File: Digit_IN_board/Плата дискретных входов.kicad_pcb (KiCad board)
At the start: 2 copper layers, 85 x 64.5 mm, 185 parts, among them J1 Prog, J2 Conn_01x02_Pin, J3 DS1013-01-14RSiB-B (1), J4 DS1013-01-10RSiB-B (1), J5 DS1013-01-10RSiB-B (2), J6 Conn_01x02_Pin, Q1 DTC114ECA, Q10 DTC114ECA (SOT-23), Q2 DTC114ECA, Q3 Si2309CDS (SOT-23), Q4 Si2309CDS (SOT-23), Q5 DTC114ECA (SOT-23), Q6 Si2309CDS (SOT-23), Q7 DTC114ECA (SOT-23), Q8 DTC114ECA (SOT-23), Q9 Si2309CDS (SOT-23), U1 ADM3485EARZ-REEL, U2 ISO6741FDWR, U3 STM32G070RBTx, U4 AM1SS-2403SJZ, U5 HEF40106B, U6 HEF40106B, U7 HEF40106B

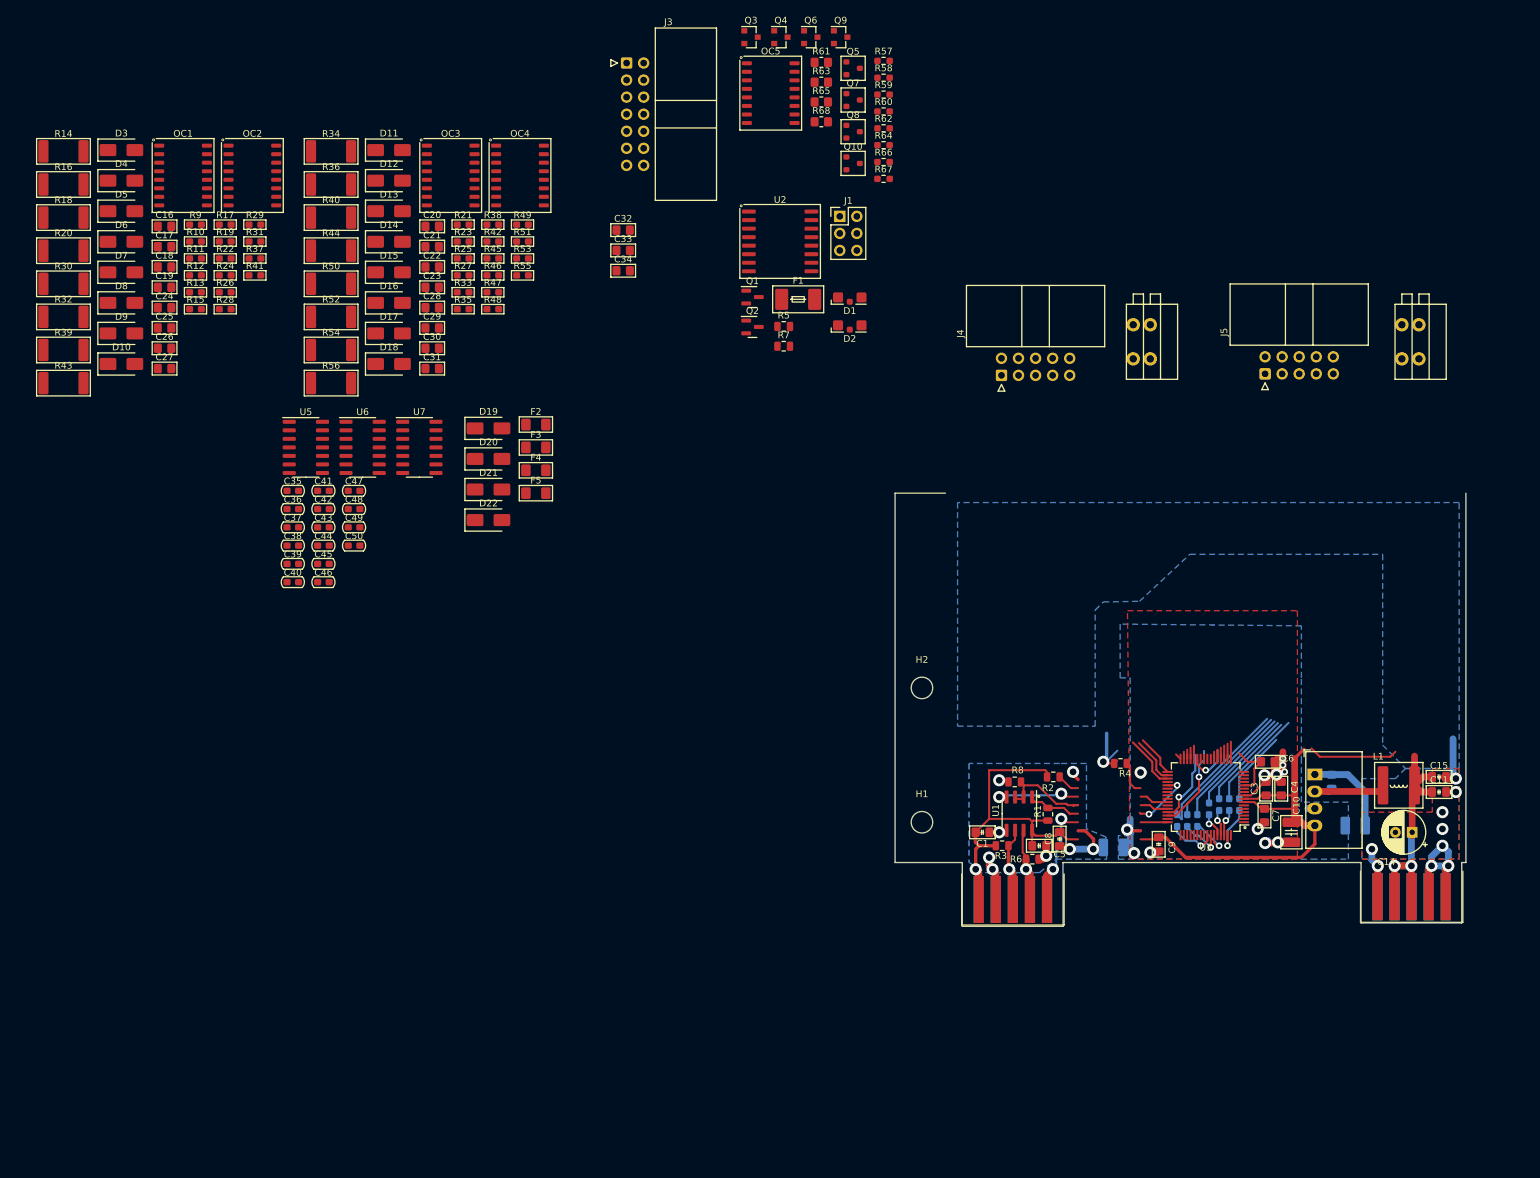
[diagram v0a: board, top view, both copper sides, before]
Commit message: Discret IN OUT schems
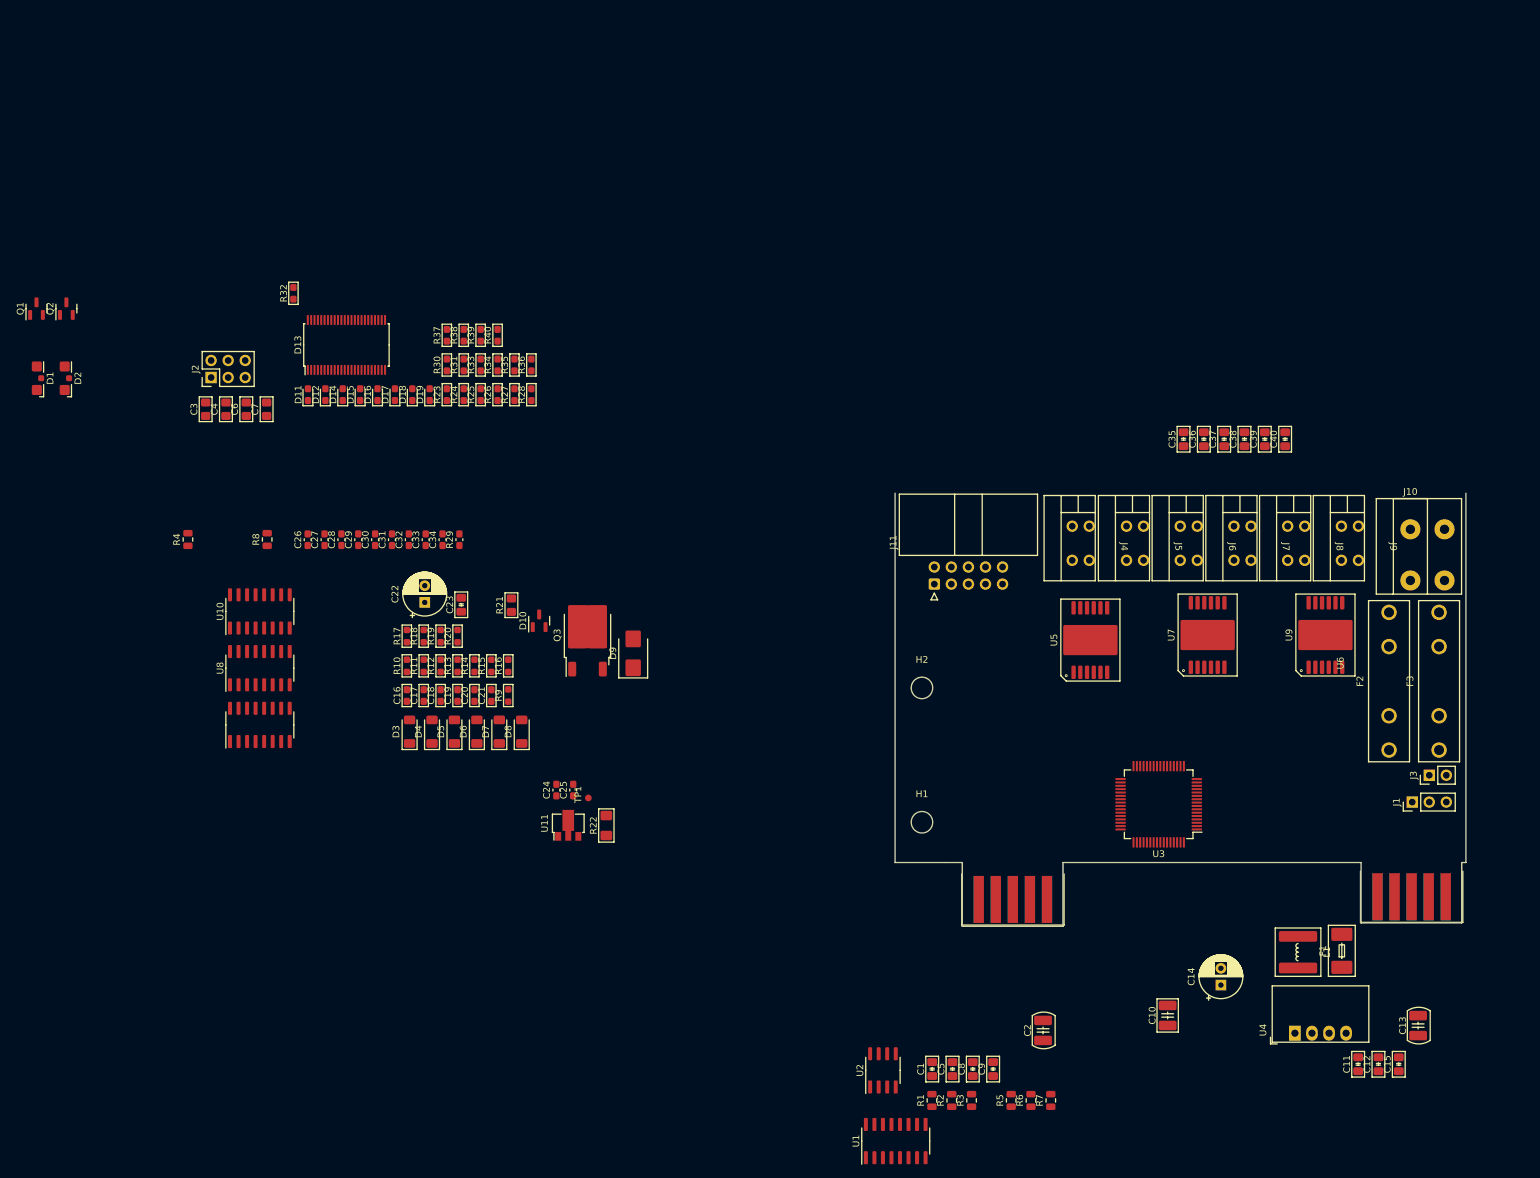
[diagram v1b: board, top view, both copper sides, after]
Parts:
- removed C41, C42, C43, C44, C45, C46, C47, C48, C49, C50: 0,01uF 50V 0603, PCM_Capacitor_SMD_US_Handsoldering_AKL:C_0603_1608Metric_Pad1.08x0.95mm
- removed D20, D21, D22: SMAJ26A, Diode_SMD:D_SMA
- removed F4, F5: 0466.500NRHF (0,5А 1206), PCM_Resistor_SMD_AKL:R_1206_3216Metric_Pad1.42x1.75mm_HandSolder
- removed OC1, OC2, OC3, OC4, OC5: IS281- 4, PCM_Package_SO_AKL:SOIC-16W_5.3x10.2mm_P1.27mm
- removed Q10, Q5, Q7, Q8: DTC114ECA (SOT-23), PCM_Package_TO_SOT_SMD_AKL:SOT-23
- removed Q4, Q6, Q9: Si2309CDS (SOT-23), PCM_4ms_Package_SOT:SOT-23
- removed the R40 at (5.02, 25.0)
- removed the R40 at (135.8, 113.0)
- removed R41, R42 (x2), R44, R45, R46 (x2), R47, R48 (x2), R49, R50, R51, R52, R53, R55: 102 0603, PCM_Resistor_SMD_AKL:R_0603_1608Metric_Pad1.05x0.95mm_HandSolder
- removed R43, R44, R50, R52, R54, R56: 102 2512, PCM_Resistor_SMD_AKL:R_2512_6332Metric_Pad1.52x3.35mm_HandSolder
- removed R57, R59, R62, R66: 103 0603, Resistor_SMD:R_0603_1608Metric_Pad0.98x0.95mm_HandSolder
- removed R58, R60, R64, R67: 473 0603, Resistor_SMD:R_0603_1608Metric_Pad0.98x0.95mm_HandSolder
- removed R61, R63, R65, R68: 201 0805, Resistor_SMD:R_0805_2012Metric_Pad1.20x1.40mm_HandSolder
- added J10: DG142R-5.08-02P-14, Connector:DG142R-5.08-02P-14, F.Cu at (165.7, 71.4)
- added J11: DS1013-01-10RSiB-B (1), Connector_IDC:IDC-Header_2x05_P2.54mm_Horizontal, F.Cu at (94.8, 79.5)
- added J7: DG141R-02, Connector:DG141R-02, F.Cu at (146.7, 74.0)
- added J8: DG141R-02, Connector:DG141R-02, F.Cu at (154.7, 74.0)
- added J9: DG141R-02, Connector:DG141R-02, F.Cu at (162.7, 74.0)
- added R40: 123 0603, PCM_Resistor_SMD_AKL:R_0603_1608Metric_Pad1.05x0.95mm_HandSolder, F.Cu at (29.8, 42.5)
- added TP1: TestPoint, PCM_4ms_TestPoint:TestPoint_D1, F.Cu at (43.3, 111.4)
- added U10: π162M30, Package_SO:SOIC-16_3.9x9.9mm_P1.27mm, F.Cu at (-5.59, 83.6)
- added U11: L78L05 (SOT89-3), Package_TO_SOT_SMD:SOT-89-3, F.Cu at (40.3, 115.2)
- added U8: π162M30, Package_SO:SOIC-16_3.9x9.9mm_P1.27mm, F.Cu at (-5.59, 92.1)
- added U9: BTS5215, PCM_Package_SO_AKL:Infineon_PG-DSO-12-9, F.Cu at (153.1, 87.1)
- C12, C13, C2: moved to F.Cu
- C16, C19, C21: value 0.1uF 100V 0805 -> 0,1uF 50V 0603; footprint PCM_Resistor_SMD_AKL:R_0805_2012Metric_Pad1.20x1.40mm_HandSolder -> PCM_Capacitor_SMD_AKL:C_0603_1608Metric_Pad1.08x0.95mm_HandSolder
- C17, C18, C20: value 0.1uF 100V 0805 -> 0,1uF 100V 0603; footprint PCM_Resistor_SMD_AKL:R_0805_2012Metric_Pad1.20x1.40mm_HandSolder -> PCM_Capacitor_SMD_AKL:C_0603_1608Metric_Pad1.08x0.95mm_HandSolder
- C22: value 0.1uF 100V 0805 -> 47uF 63V D10,5; footprint PCM_Resistor_SMD_AKL:R_0805_2012Metric_Pad1.20x1.40mm_HandSolder -> PCM_Capacitor_THT_AKL:CP_Radial_D6.3mm_P2.50mm
- C23: value 0.1uF 100V 0805 -> 0,1uF 100V 0805; footprint PCM_Resistor_SMD_AKL:R_0805_2012Metric_Pad1.20x1.40mm_HandSolder -> PCM_Capacitor_SMD_AKL:C_0805_2012Metric_Pad1.18x1.45mm_HandSolder
- C24: value 0.1uF 100V 0805 -> 0.33uF 50V 0603; footprint PCM_Resistor_SMD_AKL:R_0805_2012Metric_Pad1.20x1.40mm_HandSolder -> Capacitor_SMD:C_0603_1608Metric_Pad1.08x0.95mm_HandSolder
- C25: value 0.1uF 100V 0805 -> 0,1uF 50V 0603; footprint PCM_Resistor_SMD_AKL:R_0805_2012Metric_Pad1.20x1.40mm_HandSolder -> Capacitor_SMD:C_0603_1608Metric_Pad1.08x0.95mm_HandSolder
- C26, C27, C29, C30, C31, C32, C33, C34: value 0.1uF 100V 0805 -> 0,1uF 100V 0603; footprint PCM_Resistor_SMD_AKL:R_0805_2012Metric_Pad1.20x1.40mm_HandSolder -> Capacitor_SMD:C_0603_1608Metric_Pad1.08x0.95mm_HandSolder
- C28: value 0.1uF 100V 0805 -> 0,33uF 50V 0603; footprint PCM_Resistor_SMD_AKL:R_0805_2012Metric_Pad1.20x1.40mm_HandSolder -> Capacitor_SMD:C_0603_1608Metric_Pad1.08x0.95mm_HandSolder
- C35, C36, C37, C38, C39, C40: value 0,01uF 50V 0603 -> 0,1uF 100V 0805; footprint PCM_Capacitor_SMD_US_Handsoldering_AKL:C_0603_1608Metric_Pad1.08x0.95mm -> PCM_Capacitor_SMD_AKL:C_0805_2012Metric_Pad1.18x1.45mm_HandSolder
- D10: value SMAJ26A -> BZX84C10 (SOT-23); footprint Diode_SMD:D_SMA -> Package_TO_SOT_SMD:SOT-23
- D11, D12, D14, D15, D16, D17, D18, D19: value SMAJ26A -> LED 0603 (FYLS-0603UWC); footprint Diode_SMD:D_SMA -> LED_SMD:LED_0603_1608Metric_Pad1.05x0.95mm_HandSolder
- D13: value SMAJ26A -> ISO1I811T; footprint Diode_SMD:D_SMA -> Package_SO:TSSOP-48_6.1x12.5mm_P0.5mm
- D3, D4, D5, D6, D7, D8: value SMAJ26A -> BZV55B5V1; footprint Diode_SMD:D_SMA -> Diode_SMD:D_MiniMELF
- D9: value SMAJ26A -> SM6T30A (SMB); footprint Diode_SMD:D_SMA -> Diode_SMD:D_SMB
- F1: value 0452.500MRL -> 045201.5MRL
- F2, F3: value 0466.500NRHF (0,5А 1206) -> Fuse 5A ZH266 (2 клипсы); footprint PCM_Resistor_SMD_AKL:R_1206_3216Metric_Pad1.42x1.75mm_HandSolder -> Fuse:Fuseholder_100_series_5x20mm_D1,5
- J1: value Prog -> DebugUSART (PinHeader_01x03_P2.54mm); footprint Connector_PinHeader_2.54mm:PinHeader_2x03_P2.54mm_Vertical -> Connector_PinHeader_2.54mm:PinHeader_1x03_P2.54mm_Vertical
- J2: value Conn_01x02_Pin -> Prog (PinHeader_2x03_P2.54mm); footprint Connector:DG141V-2.54-02P -> Connector_PinHeader_2.54mm:PinHeader_2x03_P2.54mm_Vertical
- J3: value DS1013-01-14RSiB-B (1) -> Debug GPIO (PinHeader_01x02_P2.54mm); footprint Connector_IDC:IDC-Header_2x07_P2.54mm_Horizontal -> Connector_PinHeader_2.54mm:PinHeader_1x02_P2.54mm_Vertical
- J4: value DS1013-01-10RSiB-B (1) -> DG141R-02; footprint Connector_IDC:IDC-Header_2x05_P2.54mm_Horizontal -> Connector:DG141R-02
- J5: value DS1013-01-10RSiB-B (2) -> DG141R-02; footprint Connector_IDC:IDC-Header_2x05_P2.54mm_Horizontal -> Connector:DG141R-02
- J6: value Conn_01x02_Pin -> DG141R-02; footprint Connector:DG141V-2.54-02P -> Connector:DG141R-02
- Q1, Q2: value DTC114ECA -> DTC114ECA (SOT-23)
- Q3: value Si2309CDS (SOT-23) -> IRFR5305 (TO-252-2); footprint PCM_4ms_Package_SOT:SOT-23 -> Package_TO_SOT_SMD:TO-252-2
- R10, R11, R15, R19: value 102 0603 -> 123 0603; footprint PCM_Resistor_SMD_AKL:R_0603_1608Metric_Pad1.05x0.95mm_HandSolder -> PCM_Resistor_SMD_AKL:R_0603_1608Metric_Pad0.98x0.95mm_HandSolder
- R12: value 102 0603 -> 103 0603; footprint PCM_Resistor_SMD_AKL:R_0603_1608Metric_Pad1.05x0.95mm_HandSolder -> PCM_Resistor_SMD_AKL:R_0603_1608Metric_Pad0.98x0.95mm_HandSolder
- R13, R17, R9: value 102 0603 -> 302 0603; footprint PCM_Resistor_SMD_AKL:R_0603_1608Metric_Pad1.05x0.95mm_HandSolder -> PCM_Resistor_SMD_AKL:R_0603_1608Metric_Pad0.98x0.95mm_HandSolder
- R14, R18: value 102 2512 -> 123 0603; footprint PCM_Resistor_SMD_AKL:R_2512_6332Metric_Pad1.52x3.35mm_HandSolder -> PCM_Resistor_SMD_AKL:R_0603_1608Metric_Pad0.98x0.95mm_HandSolder
- R16, R20: value 102 2512 -> 103 0603; footprint PCM_Resistor_SMD_AKL:R_2512_6332Metric_Pad1.52x3.35mm_HandSolder -> PCM_Resistor_SMD_AKL:R_0603_1608Metric_Pad0.98x0.95mm_HandSolder
- R21: value 102 0603 -> 103 0805; footprint PCM_Resistor_SMD_AKL:R_0603_1608Metric_Pad1.05x0.95mm_HandSolder -> PCM_Resistor_SMD_AKL:R_0805_2012Metric_Pad1.20x1.40mm_HandSolder
- R22: value 102 0603 -> 621 1206; footprint PCM_Resistor_SMD_AKL:R_0603_1608Metric_Pad1.05x0.95mm_HandSolder -> PCM_Resistor_SMD_AKL:R_1206_3216Metric_Pad1.42x1.75mm_HandSolder
- R23, R25, R27, R33, R35, R37: value 102 0603 -> 202 0603
- R24, R26, R28, R31, R38: value 102 0603 -> 123 0603
- R29: value 102 0603 -> 204 0603; footprint PCM_Resistor_SMD_AKL:R_0603_1608Metric_Pad1.05x0.95mm_HandSolder -> Capacitor_SMD:C_0603_1608Metric_Pad1.08x0.95mm_HandSolder
- R30, R39: value 102 2512 -> 202 0603; footprint PCM_Resistor_SMD_AKL:R_2512_6332Metric_Pad1.52x3.35mm_HandSolder -> PCM_Resistor_SMD_AKL:R_0603_1608Metric_Pad1.05x0.95mm_HandSolder
- R32: value 102 2512 -> 330 0603; footprint PCM_Resistor_SMD_AKL:R_2512_6332Metric_Pad1.52x3.35mm_HandSolder -> PCM_Resistor_SMD_AKL:R_0603_1608Metric_Pad1.05x0.95mm_HandSolder
- R34, R36: value 102 2512 -> 123 0603; footprint PCM_Resistor_SMD_AKL:R_2512_6332Metric_Pad1.52x3.35mm_HandSolder -> PCM_Resistor_SMD_AKL:R_0603_1608Metric_Pad1.05x0.95mm_HandSolder
- R4: value 472 0805 -> 151 0805
- R5: value 151 0805 -> 472 0805
- R7: value 151 0805 -> 103 0805
- R8: value 103 0805 -> 151 0805
- U1: value ADM3485EARZ-REEL -> π141M3x; footprint Package_SO:SOIC-8_3.9x4.9mm_P1.27mm -> Package_SO:SOIC-16_3.9x9.9mm_P1.27mm
- U2: value ISO6741FDWR -> ADM3485EARZ-REEL (SOIC-8); footprint PCM_Package_SO_AKL:SOIC-16W_7.5x10.3mm_P1.27mm -> Package_SO:SOIC-8_3.9x4.9mm_P1.27mm
- U3: value STM32G070RBTx -> STM32G070RBTx (LQFP-64)
- U5, U7: value HEF40106B -> BTS5215; footprint Package_SO:SO-14_3.9x8.65mm_P1.27mm -> PCM_Package_SO_AKL:Infineon_PG-DSO-12-9
- U6: value HEF40106B -> π162M30; footprint Package_SO:SO-14_3.9x8.65mm_P1.27mm -> Package_SO:SOIC-16_3.9x9.9mm_P1.27mm
- moved C3 167.7 mm to (-13.7, 53.5)
- moved C4 167.0 mm to (-10.6, 53.5)
- moved C6 160.9 mm to (-7.61, 53.5), turned to 90 degrees
- moved C7 160.4 mm to (-4.59, 53.5), turned to 90 degrees
- moved J3 159.8 mm to (168.5, 108.0), turned to 90 degrees
- moved C40 149.3 mm to (147.1, 58.0), turned to 90 degrees
- moved C39 145.9 mm to (144.1, 58.0), turned to 90 degrees
- moved R4 142.8 mm to (-16.3, 72.9), turned to 90 degrees
- moved C38 142.6 mm to (141.0, 58.0), turned to 90 degrees
- moved F3 141.8 mm to (170.0, 104.2), turned to 90 degrees
- moved C37 139.3 mm to (138.0, 58.0), turned to 90 degrees
- moved J2 137.5 mm to (-12.8, 48.8), turned to 90 degrees
- moved C36 136.1 mm to (135.0, 58.0), turned to 90 degrees
- moved F2 136.0 mm to (162.6, 104.2), turned to 90 degrees
- moved C35 132.9 mm to (131.9, 58.0), turned to 90 degrees
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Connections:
- C16 pad 1: /IN_Detector/OUT1_1 -> GNDD
- C16 pad 2: GNDA -> +3V3
- C17 pad 1: /IN_Detector/OUT1_2 -> GND2
- C17 pad 2: GNDA -> +5V
- C18 pad 1: /IN_Detector/OUT1_3 -> GND2
- C18 pad 2: GNDA -> +5V
- C19 pad 1: /IN_Detector/OUT1_4 -> GNDD
- C19 pad 2: GNDA -> +3V3
- C20 pad 1: /IN_Detector/OUT2_1 -> GND2
- C20 pad 2: GNDA -> +5V
- C21 pad 1: /IN_Detector/OUT2_2 -> GNDD
- C21 pad 2: GNDA -> +3V3
- C22 pad 1: /IN_Detector/OUT2_3 -> +24V
- C22 pad 2: GNDA -> GND2
- C23 pad 1: /IN_Detector/OUT2_4 -> +24V
- C23 pad 2: GNDA -> GND2
- C24 pad 1: /IN_Detector/OUT1_5 -> Net-(U11-IN)
- C24 pad 2: GNDA -> GND2
- C25 pad 1: /IN_Detector/OUT1_6 -> +5V
- C25 pad 2: GNDA -> GND2
- C26 pad 1: /IN_Detector/OUT1_7 -> /Descret Input/OUT1_1
- C26 pad 2: GNDA -> GND2
- C27 pad 1: /IN_Detector/OUT1_8 -> /Descret Input/OUT1_2
- C27 pad 2: GNDA -> GND2
- C28 pad 1: /IN_Detector/OUT2_5 -> +3V3
- C28 pad 2: GNDA -> GNDD
- C29 pad 1: /IN_Detector/OUT2_6 -> /Descret Input/OUT1_3
- C29 pad 2: GNDA -> GND2
- C30 pad 1: /IN_Detector/OUT2_7 -> /Descret Input/OUT1_4
- C30 pad 2: GNDA -> GND2
- C31 pad 1: /IN_Detector/OUT2_8 -> /Descret Input/OUT1_5
- C31 pad 2: GNDA -> GND2
- C32 pad 1: +3V3 -> /Descret Input/OUT1_6
- C32 pad 2: GNDD -> GND2
- C33 pad 1: +3V3 -> /Descret Input/OUT1_7
- C33 pad 2: GNDD -> GND2
- C34 pad 1: +3V3 -> /Descret Input/OUT1_8
- C34 pad 2: GNDD -> GND2
- C35 pad 1: /IN_Detector/D2_1 -> GND2
- C35 pad 2: GNDD -> /+24_FT_1
- C36 pad 1: /IN_Detector/D2_2 -> GND2
- C36 pad 2: GNDD -> /DiscretOut/OUT2
- C37 pad 1: /IN_Detector/D2_3 -> GND2
- C37 pad 2: GNDD -> /DiscretOut/OUT3
- C38 pad 1: /IN_Detector/D2_4 -> GND2
- C38 pad 2: GNDD -> /DiscretOut/OUT4
- C39 pad 1: /IN_Detector/D2_5 -> GND2
- C39 pad 2: GNDD -> /DiscretOut/OUT5
- C40 pad 1: /IN_Detector/D2_6 -> GND2
- C40 pad 2: GNDD -> /DiscretOut/OUT6
- D10 pad 1: /IN_Detector/OUT1_8 -> Net-(D10-A)
- D10 pad 2: GNDA -> unconnected-(D10-NC-Pad2)
- D11 pad 1: /IN_Detector/OUT2_1 -> GND2
- D11 pad 2: GNDA -> /Descret Input/OUT1_L
- D12 pad 1: /IN_Detector/OUT2_2 -> GND2
- D12 pad 2: GNDA -> /Descret Input/OUT2_L
- D13 pad 1: /IN_Detector/OUT2_3 -> GNDD
- D13 pad 2: GNDA -> GNDD
- D14 pad 1: /IN_Detector/OUT2_4 -> GND2
- D14 pad 2: GNDA -> /Descret Input/OUT3_L
- D15 pad 1: /IN_Detector/OUT2_5 -> GND2
- D15 pad 2: GNDA -> /Descret Input/OUT4_L
- D16 pad 1: /IN_Detector/OUT2_6 -> GND2
- D16 pad 2: GNDA -> /Descret Input/OUT5_L
- D17 pad 1: /IN_Detector/OUT2_7 -> GND2
- D17 pad 2: GNDA -> /Descret Input/OUT6_L
- D18 pad 1: /IN_Detector/OUT2_8 -> GND2
- D18 pad 2: GNDA -> /Descret Input/OUT7_L
- D19 pad 1: Net-(D19-A1) -> GND2
- D19 pad 2: GNDA -> /Descret Input/OUT8_L
- D3 pad 1: /IN_Detector/OUT1_1 -> /DiscretOut/OUT1_1
- D3 pad 2: GNDA -> GND2
- D4 pad 1: /IN_Detector/OUT1_2 -> /DiscretOut/OUT2_1
- D4 pad 2: GNDA -> GND2
- D5 pad 1: /IN_Detector/OUT1_3 -> /DiscretOut/OUT3_1
- D5 pad 2: GNDA -> GND2
- D6 pad 1: /IN_Detector/OUT1_4 -> /DiscretOut/OUT4_1
- D6 pad 2: GNDA -> GND2
- D7 pad 1: /IN_Detector/OUT1_5 -> /DiscretOut/OUT6_1
- D7 pad 2: GNDA -> GND2
- D8 pad 1: /IN_Detector/OUT1_6 -> /DiscretOut/OUT6_1
- D8 pad 2: GNDA -> GND2
- D9 pad 1: /IN_Detector/OUT1_7 -> Net-(D9-A1)
- D9 pad 2: GNDA -> GND2
- F2 pad 1: Net-(D19-A1) -> Net-(D9-A1)
- F2 pad 2: /IN_Detector/+24_LED_1 -> Net-(J10-Pin_1)
- F3 pad 1: Net-(D20-A1) -> GND2
- F3 pad 2: /IN_Detector/+24_FT_1 -> Net-(J10-Pin_2)
- J1 pad 1: +3V3 -> /UART_TX
- J1 pad 2: /SWDIO -> /UART_RX
- J1 pad 3: /SWCLK -> /UART_DE
- J2 pad 1: unconnected-(J2-Pin_1-Pad1) -> +3V3
- J2 pad 2: unconnected-(J2-Pin_2-Pad2) -> /SWDIO
- J3 pad 1: /IN_Detector/OUT2_1 -> /GPIO1
- J3 pad 2: /IN_Detector/OUT2_2 -> /GPIO2
- J4 pad 1: /IN_Detector/OUT1_1 -> /+24_FT_1
- J4 pad 2: /IN_Detector/OUT1_2 -> GND2
- J5 pad 1: unconnected-(J5-Pin_1-Pad1) -> /DiscretOut/OUT2
- J5 pad 2: unconnected-(J5-Pin_2-Pad2) -> GND2
- J6 pad 1: unconnected-(J6-Pin_1-Pad1) -> /DiscretOut/OUT3
- J6 pad 2: unconnected-(J6-Pin_2-Pad2) -> GND2
- Q3 pad 1: Net-(Q3-G) -> Net-(D10-A)
- Q3 pad 2: +24V -> Net-(D9-A1)
- Q3 pad 3: Net-(D19-A1) -> +24V
- R1 pad 1: Net-(U1-RO) -> Net-(U1-VID)
- R10 pad 1: +3V3 -> /DiscretOut/OUT1_1
- R10 pad 2: Net-(OC1-Pad14) -> /+24_FT_1
- R11 pad 1: +3V3 -> /DiscretOut/OUT2_1
- R11 pad 2: Net-(OC1-Pad12) -> /DiscretOut/OUT2
- R12 pad 1: +3V3 -> GND2
- R12 pad 2: Net-(OC1-Pad10) -> /DiscretOut/OUT2_1
- R13 pad 1: Net-(OC1-Pad16) -> GND2
- R13 pad 2: /IN_Detector/D1_1 -> /DiscretOut/OUT3_1
- R14 pad 1: GNDA -> /DiscretOut/OUT3_1
- R14 pad 2: Net-(OC1-Pad2) -> /DiscretOut/OUT3
- R15 pad 1: Net-(OC1-Pad14) -> /DiscretOut/OUT4_1
- R15 pad 2: /IN_Detector/D1_2 -> /DiscretOut/OUT4
- R16 pad 1: GNDA -> GND2
- R16 pad 2: Net-(OC1-Pad4) -> /DiscretOut/OUT4_1
- R17 pad 1: Net-(OC1-Pad12) -> GND2
- R17 pad 2: /IN_Detector/D1_3 -> /DiscretOut/OUT6_1
- R18 pad 1: GNDA -> /DiscretOut/OUT6_1
- R18 pad 2: Net-(OC1-Pad6) -> /DiscretOut/OUT5
- R19 pad 1: Net-(OC1-Pad10) -> /DiscretOut/OUT6_1
- R19 pad 2: /IN_Detector/D1_4 -> /DiscretOut/OUT6
- R2 pad 1: Net-(U2-EN2) -> Net-(U1-VE2)
- R20 pad 1: GNDA -> GND2
- R20 pad 2: Net-(OC1-Pad8) -> /DiscretOut/OUT6_1
- R21 pad 1: +3V3 -> Net-(D10-A)
- R21 pad 2: Net-(OC3-Pad16) -> GND2
- R22 pad 1: +3V3 -> Net-(U11-IN)
- R22 pad 2: Net-(OC2-Pad16) -> +24V
- R23 pad 1: +3V3 -> /Descret Input/OUT1_H
- R23 pad 2: Net-(OC3-Pad14) -> /Descret Input/OUT1_1
- R24 pad 1: +3V3 -> /Descret Input/OUT1_1
- R24 pad 2: Net-(OC2-Pad14) -> /Descret Input/OUT1_L
- R25 pad 1: +3V3 -> /Descret Input/OUT2_H
- R25 pad 2: Net-(OC3-Pad12) -> /Descret Input/OUT1_2
- R26 pad 1: +3V3 -> /Descret Input/OUT1_2
- R26 pad 2: Net-(OC2-Pad12) -> /Descret Input/OUT2_L
- R27 pad 1: +3V3 -> /Descret Input/OUT3_H
- R27 pad 2: Net-(OC3-Pad10) -> /Descret Input/OUT1_3
- R28 pad 1: +3V3 -> /Descret Input/OUT1_3
- R28 pad 2: Net-(OC2-Pad10) -> /Descret Input/OUT3_L
- R29 pad 1: Net-(OC2-Pad16) -> GNDD
- R29 pad 2: /IN_Detector/D1_5 -> Net-(D13-Rosc)
- R30 pad 1: GNDA -> /Descret Input/OUT4_H
- R30 pad 2: Net-(OC2-Pad2) -> /Descret Input/OUT1_4
- R31 pad 1: Net-(OC2-Pad14) -> /Descret Input/OUT1_4
- R31 pad 2: /IN_Detector/D1_6 -> /Descret Input/OUT4_L
- R32 pad 1: GNDA -> GND2
- R32 pad 2: Net-(OC2-Pad4) -> Net-(D13-TS)
- R33 pad 1: Net-(OC3-Pad16) -> /Descret Input/OUT5_H
- R33 pad 2: /IN_Detector/D2_1 -> /Descret Input/OUT1_5
- R34 pad 1: GNDA -> /Descret Input/OUT1_5
- R34 pad 2: Net-(OC3-Pad2) -> /Descret Input/OUT5_L
- R35 pad 1: Net-(OC3-Pad14) -> /Descret Input/OUT6_H
- R35 pad 2: /IN_Detector/D2_2 -> /Descret Input/OUT1_6
- R36 pad 1: GNDA -> /Descret Input/OUT1_6
- R36 pad 2: Net-(OC3-Pad4) -> /Descret Input/OUT6_L
- R37 pad 1: Net-(OC2-Pad12) -> /Descret Input/OUT7_H
- R37 pad 2: /IN_Detector/D1_7 -> /Descret Input/OUT1_7
- R38 pad 1: Net-(OC3-Pad12) -> /Descret Input/OUT1_7
- R38 pad 2: /IN_Detector/D2_3 -> /Descret Input/OUT7_L
- R39 pad 1: GNDA -> /Descret Input/OUT8_H
- R39 pad 2: Net-(OC2-Pad6) -> /Descret Input/OUT1_8
- R4 pad 1: +3V3 -> Net-(D1-A)
- R4 pad 2: Net-(U2-EN1) -> +3V3
- R5 pad 1: Net-(D1-A) -> +3V3
- R5 pad 2: +3V3 -> Net-(U1-VE1)
- R7 pad 1: +3V3 -> GND1
- R7 pad 2: Net-(D2-A) -> Net-(U1-VOC)
- R8 pad 1: GND1 -> +3V3
- R8 pad 2: Net-(U1-DE) -> Net-(D2-A)
- R9 pad 1: +3V3 -> GND2
- R9 pad 2: Net-(OC1-Pad16) -> /DiscretOut/OUT1_1
- U1 pad 1: Net-(U1-RO) -> +3V3
- U1 pad 2: Net-(U1-DE) -> GNDD
- U1 pad 3: Net-(U1-DE) -> /RTS_cont
- U1 pad 4: Net-(U1-DI) -> /TX_USART_1
- U1 pad 5: GND1 -> /DE_USART_1
- U1 pad 6: Net-(RS1-Pin_3) -> /RX_USART_1
- U1 pad 7: Net-(RS1-Pin_4) -> Net-(U1-VE1)
- U1 pad 8: /+3.3VRS485 -> GNDD
- U2 pad 1: +3V3 -> Net-(U1-VID)
- U2 pad 2: GNDD -> Net-(U1-VOC)
- U2 pad 3: /RTS_cont -> Net-(U1-VOC)
- U2 pad 4: /RO -> Net-(U1-VOB)
- U2 pad 5: /DE -> GND1
- U2 pad 6: /DI -> Net-(RS1-Pin_3)
- U2 pad 7: Net-(U2-EN1) -> Net-(RS1-Pin_4)
- U2 pad 8: GNDD -> /+3.3VRS485
- U3 pad 1: unconnected-(U3-PC11-Pad1) -> /ST6_cont
- U3 pad 17: /LED_ON_1 -> unconnected-(U3-PA0-Pad17)
- U3 pad 18: /FT_ON_1 -> unconnected-(U3-PA1-Pad18)
- U3 pad 19: /LED_ON_2 -> unconnected-(U3-PA2-Pad19)
- U3 pad 2: unconnected-(U3-PC12-Pad2) -> /OUT6_1_cont
- U3 pad 20: /FT_ON_2 -> Net-(Q1-B)
- U3 pad 21: Net-(Q1-B) -> Net-(Q2-B)
- U3 pad 22: Net-(Q2-B) -> /ERR
- U3 pad 23: unconnected-(U3-PA6-Pad23) -> /DS0
- U3 pad 24: unconnected-(U3-PA7-Pad24) -> /DS1
- U3 pad 25: unconnected-(U3-PC4-Pad25) -> /GPIO1
- U3 pad 26: unconnected-(U3-PC5-Pad26) -> /GPIO2
- U3 pad 27: /D11 -> /D0
- U3 pad 28: /D28 -> /D1
- U3 pad 29: /D27 -> /D2
- U3 pad 30: /D26 -> /D3
- U3 pad 31: /D25 -> /D4
- U3 pad 32: /D24 -> /D5
- U3 pad 33: /D23 -> /D6
- U3 pad 34: /D22 -> /D7
- U3 pad 35: /D21 -> unconnected-(U3-PB15-Pad35)
- U3 pad 37: /RO -> /TX_USART_1
- U3 pad 39: unconnected-(U3-PC7-Pad39) -> /UART_DE
- U3 pad 40: unconnected-(U3-PD8-Pad40) -> /UART_TX
- U3 pad 41: unconnected-(U3-PD9-Pad41) -> /UART_RX
- U3 pad 42: /DI -> /RX_USART_1
- U3 pad 44: /DE -> /DE_USART_1
- U3 pad 49: unconnected-(U3-PC9-Pad49) -> /ON_OUT1
- U3 pad 50: unconnected-(U3-PD0-Pad50) -> /ST1_cont
- U3 pad 51: unconnected-(U3-PD1-Pad51) -> /OUT1_1_cont
- U3 pad 52: unconnected-(U3-PD2-Pad52) -> /ON_OUT2
- U3 pad 53: unconnected-(U3-PD3-Pad53) -> /ST2_cont
- U3 pad 54: unconnected-(U3-PD4-Pad54) -> /OUT2_1_cont
- U3 pad 55: unconnected-(U3-PD5-Pad55) -> /ON_OUT3
- U3 pad 56: unconnected-(U3-PD6-Pad56) -> /ST3_cont
- U3 pad 57: /D12 -> /OUT3_1_cont
- U3 pad 58: /D13 -> /ON_OUT4
- U3 pad 59: /D14 -> /ST4_cont
- U3 pad 60: /D15 -> /OUT4_1_cont
- U3 pad 61: /D16 -> /ON_OUT5
- U3 pad 62: /D17 -> /ST5_cont
- U3 pad 63: /D18 -> /OUT5_1_cont
- U3 pad 64: unconnected-(U3-PC10-Pad64) -> /ON_OUT6
- U5 pad 1: /IN_Detector/D2_1 -> GND2
- U5 pad 10: /D25 -> /+24_FT_1
- U5 pad 11: /IN_Detector/D2_5 -> unconnected-(U5-NC-Pad11)
- U5 pad 12: /D26 -> +24V
- U5 pad 13: /IN_Detector/D2_6 -> +24V
- U5 pad 2: /D21 -> /DiscretOut/IN1
- U5 pad 3: /IN_Detector/D2_2 -> /DiscretOut/ST1
- U5 pad 4: /D22 -> /DiscretOut/IN2
- U5 pad 5: /IN_Detector/D2_3 -> /DiscretOut/ST2
- U5 pad 6: /D23 -> +24V
- U5 pad 7: GNDD -> unconnected-(U5-NC-Pad7)
- U5 pad 8: /D24 -> /DiscretOut/OUT2
- U5 pad 9: /IN_Detector/D2_4 -> unconnected-(U5-NC-Pad9)
- U6 pad 1: /IN_Detector/D2_7 -> +5V
- U6 pad 10: /D13 -> /ON_OUT2
- U6 pad 11: /IN_Detector/D1_3 -> /ON_OUT1
- U6 pad 12: /D14 -> /OUT1_1_cont
- U6 pad 13: /IN_Detector/D1_4 -> /ST1_cont
- U6 pad 14: +3V3 -> /ST2_cont
- U6 pad 2: /D27 -> /DiscretOut/OUT2_1
- U6 pad 3: /IN_Detector/D2_8 -> /DiscretOut/ST2
- U6 pad 4: /D28 -> /DiscretOut/ST1
- U6 pad 5: /IN_Detector/D1_1 -> /DiscretOut/OUT1_1
- U6 pad 6: /D11 -> /DiscretOut/IN1
- U6 pad 7: GNDD -> /DiscretOut/IN2
- U6 pad 8: /D12 -> GND2
- U6 pad 9: /IN_Detector/D1_2 -> GNDD
- U7 pad 1: /IN_Detector/D1_5 -> GND2
- U7 pad 10: unconnected-(U7-Pad10) -> /DiscretOut/OUT3
- U7 pad 12: unconnected-(U7-Pad12) -> +24V
- U7 pad 13: unconnected-(U7-Pad13) -> +24V
- U7 pad 2: /D15 -> /DiscretOut/IN3
- U7 pad 3: /IN_Detector/D1_6 -> /DiscretOut/ST3
- U7 pad 4: /D16 -> /DiscretOut/IN4
- U7 pad 5: /IN_Detector/D1_7 -> /DiscretOut/ST4
- U7 pad 6: /D17 -> +24V
- U7 pad 7: GNDD -> unconnected-(U7-NC-Pad7)
- U7 pad 8: /D18 -> /DiscretOut/OUT4
- U7 pad 9: /IN_Detector/D1_8 -> unconnected-(U7-NC-Pad9)
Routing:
- net +3V3: track 69.9 -> 0.00 mm, vias 1 -> 0
- net GNDA: track 62.5 -> 0.00 mm, vias 9 -> 0
- net /+3.3VRS485: track 58.9 -> 0.00 mm, vias 1 -> 0
- net +24V: track 48.8 -> 0.00 mm, vias 2 -> 0
- net GNDD: track 36.2 -> 0.00 mm, vias 12 -> 0
- net GND1: track 25.0 -> 0.00 mm, vias 8 -> 0
- net /RTS: track 21.8 -> 0.00 mm, vias 2 -> 0
- net Net-(OC3-Pad13): track 21.7 -> 0.00 mm
- net Net-(OC3-Pad11): track 19.3 -> 0.00 mm
- net Net-(OC3-Pad9): track 18.6 -> 0.00 mm
- net Net-(OC4-Pad15): track 16.1 -> 0.00 mm
- net Net-(RS1-Pin_4): track 15.5 -> 0.00 mm, vias 1 -> 0
- net Net-(RS1-Pin_3): track 15.4 -> 0.00 mm, vias 1 -> 0
- net Net-(OC4-Pad11): track 15.0 -> 0.00 mm
- net Net-(OC4-Pad13): track 14.8 -> 0.00 mm
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- removed copper zone on B.Cu, net GND1
- removed copper zone on B.Cu, net GNDA
- removed copper zone on F.Cu, net GNDA
- removed copper zone on B.Cu, net GNDD
- removed copper zone on F.Cu, net GNDD
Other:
- outline, holes or cut-outs redrawn

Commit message: DIgit_IN renew schems
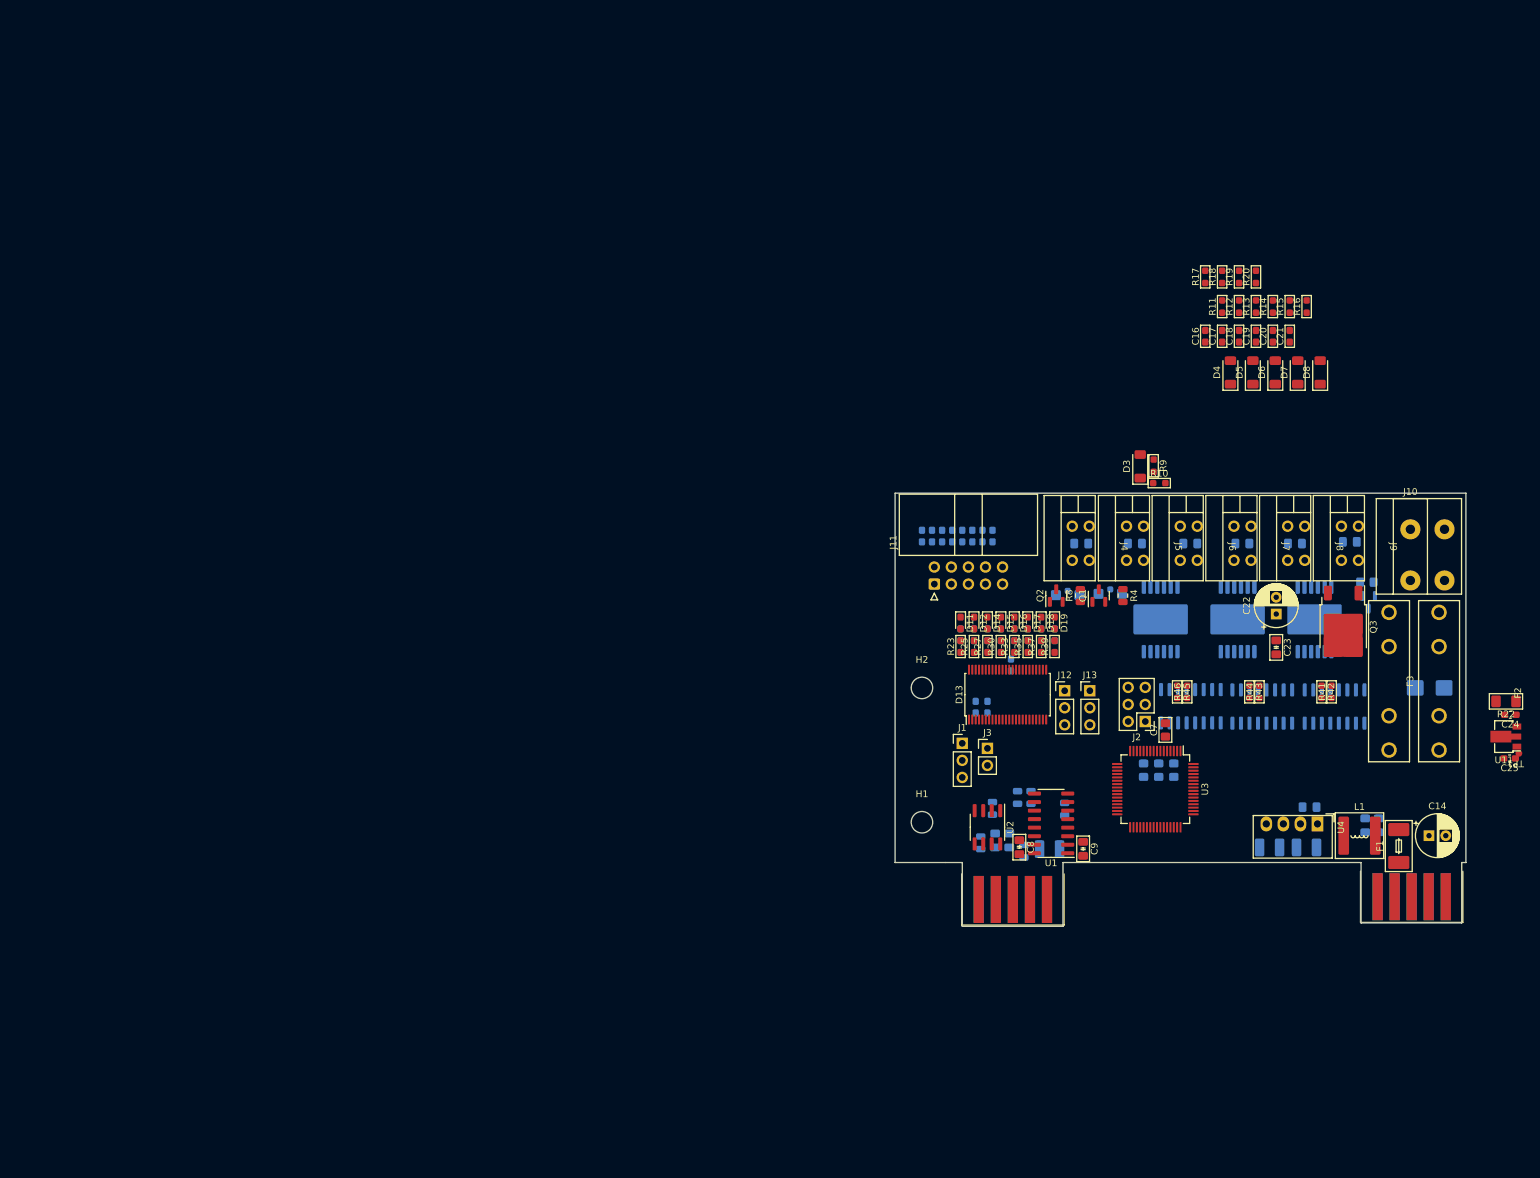
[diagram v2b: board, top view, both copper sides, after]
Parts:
- added J12: DS0, Connector_PinHeader_2.54mm:PinHeader_1x03_P2.54mm_Vertical, F.Cu at (114.2, 95.4)
- added J13: DS0, Connector_PinHeader_2.54mm:PinHeader_1x03_P2.54mm_Vertical, F.Cu at (118.0, 95.4)
- added R41: 103 0603, PCM_Resistor_SMD_AKL:R_0603_1608Metric_Pad0.98x0.95mm_HandSolder, F.Cu at (154.0, 95.6)
- added R42: 103 0603, PCM_Resistor_SMD_AKL:R_0603_1608Metric_Pad0.98x0.95mm_HandSolder, F.Cu at (152.5, 95.6)
- added R43: 103 0603, PCM_Resistor_SMD_AKL:R_0603_1608Metric_Pad0.98x0.95mm_HandSolder, F.Cu at (141.8, 95.6)
- added R44: 103 0603, PCM_Resistor_SMD_AKL:R_0603_1608Metric_Pad0.98x0.95mm_HandSolder, F.Cu at (143.2, 95.6)
- added R45: 103 0603, PCM_Resistor_SMD_AKL:R_0603_1608Metric_Pad0.98x0.95mm_HandSolder, F.Cu at (131.0, 95.6)
- added R46: 103 0603, PCM_Resistor_SMD_AKL:R_0603_1608Metric_Pad0.98x0.95mm_HandSolder, F.Cu at (132.5, 95.6)
- C1, C10, C11, C12, C13, C15, C2, C26, C27, C28, C29, C3, C30, C31, C32, C33, C34, C35, C36, C37, C38, C39, C4, C40, C5, C6, D1, D10, D2, D9, R1, R2, R21, R24, R26, R28, R29, R3, R31, R32, R34, R36, R38, R40, R5, R6, R7, U10, U5, U6, U7, U8, U9: moved to B.Cu
- U4: footprint Converter_DCDC:Converter_DCDC_Murata_MEE3SxxxxSC_THT -> Converter_DCDC:Converter_DCDC_Murata_MEE1SxxxxSC_THT
- moved Q1 163.9 mm to (119.3, 81.2)
- moved D1 163.6 mm to (121.0, 81.5), turned to 0 degrees
- moved U10 160.7 mm to (154.4, 97.8), turned to -90 degrees
- moved Q2 153.5 mm to (113.0, 81.2)
- moved D2 153.4 mm to (114.7, 81.7), turned to 0 degrees
- moved C3 151.7 mm to (128.2, 107.2), turned to -90 degrees
- moved C4 151.0 mm to (130.5, 107.2), turned to -90 degrees
- moved U8 149.4 mm to (143.7, 97.8), turned to -90 degrees
- moved J2 148.2 mm to (126.2, 100.0), turned to 180 degrees
- moved C6 144.0 mm to (126.0, 107.2), turned to -90 degrees
- moved C24 142.5 mm to (180.6, 99.0), turned to 180 degrees
- moved C7 142.1 mm to (129.2, 101.2)
- moved U11 139.9 mm to (179.6, 102.2), turned to 180 degrees
- moved C25 139.5 mm to (180.5, 105.5), turned to 180 degrees
- moved R4 139.5 mm to (122.9, 81.2), turned to -90 degrees
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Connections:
- C22 pad 1: +24V -> /DiscretOut/24V_OUT
- C23 pad 1: +24V -> /DiscretOut/24V_OUT
- D10 pad 3: +24V -> /DiscretOut/24V_OUT
- D13 pad 19: /DS0 -> Net-(D13-DS0)
- D13 pad 20: /DS1 -> Net-(D13-DS1)
- J1 pad 1: /UART_TX -> /UART_DE
- J1 pad 2: /UART_RX -> /UART_TX
- J1 pad 3: /UART_DE -> /UART_RX
- Q3 pad 3: +24V -> /DiscretOut/24V_OUT
- R22 pad 2: +24V -> /DiscretOut/24V_OUT
- U3 pad 1: /ST6_cont -> /ST2_cont
- U3 pad 2: /OUT6_1_cont -> /OUT2_1_cont
- U3 pad 23: /DS0 -> unconnected-(U3-PA6-Pad23)
- U3 pad 24: /DS1 -> unconnected-(U3-PA7-Pad24)
- U3 pad 27: /D0 -> /D7
- U3 pad 28: /D1 -> /D6
- U3 pad 29: /D2 -> /D5
- U3 pad 30: /D3 -> /D4
- U3 pad 31: /D4 -> /D3
- U3 pad 32: /D5 -> /D2
- U3 pad 33: /D6 -> /D1
- U3 pad 34: /D7 -> /D0
- U3 pad 49: /ON_OUT1 -> /ON_OUT6
- U3 pad 50: /ST1_cont -> /ON_OUT5
- U3 pad 51: /OUT1_1_cont -> /OUT5_1_cont
- U3 pad 52: /ON_OUT2 -> /ST5_cont
- U3 pad 53: /ST2_cont -> /OUT6_1_cont
- U3 pad 54: /OUT2_1_cont -> /ST6_cont
- U3 pad 55: /ON_OUT3 -> /ON_OUT4
- U3 pad 56: /ST3_cont -> /ON_OUT3
- U3 pad 58: /ON_OUT4 -> /ST3_cont
- U3 pad 61: /ON_OUT5 -> /ON_OUT2
- U3 pad 62: /ST5_cont -> /ON_OUT1
- U3 pad 63: /OUT5_1_cont -> /OUT1_1_cont
- U3 pad 64: /ON_OUT6 -> /ST1_cont
- U5 pad 10: /+24_FT_1 -> /DiscretOut/OUT2
- U5 pad 12: +24V -> /DiscretOut/24V_OUT
- U5 pad 13: +24V -> /DiscretOut/24V_OUT
- U5 pad 2: /DiscretOut/IN1 -> /DiscretOut/IN2
- U5 pad 3: /DiscretOut/ST1 -> /DiscretOut/ST2
- U5 pad 4: /DiscretOut/IN2 -> /DiscretOut/IN1
- U5 pad 5: /DiscretOut/ST2 -> /DiscretOut/ST1
- U5 pad 6: +24V -> /DiscretOut/24V_OUT
- U5 pad 8: /DiscretOut/OUT2 -> /+24_FT_1
- U7 pad 10: /DiscretOut/OUT3 -> /DiscretOut/OUT4
- U7 pad 12: +24V -> /DiscretOut/24V_OUT
- U7 pad 13: +24V -> /DiscretOut/24V_OUT
- U7 pad 2: /DiscretOut/IN3 -> /DiscretOut/IN4
- U7 pad 3: /DiscretOut/ST3 -> /DiscretOut/ST4
- U7 pad 4: /DiscretOut/IN4 -> /DiscretOut/IN3
- U7 pad 5: /DiscretOut/ST4 -> /DiscretOut/ST3
- U7 pad 6: +24V -> /DiscretOut/24V_OUT
- U7 pad 8: /DiscretOut/OUT4 -> /DiscretOut/OUT3
- U9 pad 10: /DiscretOut/OUT5 -> /DiscretOut/OUT6
- U9 pad 12: +24V -> /DiscretOut/24V_OUT
- U9 pad 13: +24V -> /DiscretOut/24V_OUT
- U9 pad 2: /DiscretOut/IN5 -> /DiscretOut/IN6
- U9 pad 3: /DiscretOut/ST5 -> /DiscretOut/ST6
- U9 pad 4: /DiscretOut/IN6 -> /DiscretOut/IN5
- U9 pad 5: /DiscretOut/ST6 -> /DiscretOut/ST5
- U9 pad 6: +24V -> /DiscretOut/24V_OUT
- U9 pad 8: /DiscretOut/OUT6 -> /DiscretOut/OUT5
